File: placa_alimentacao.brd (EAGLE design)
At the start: 55.5 x 32.4 mm, 8 parts, among them IC1 7803TV

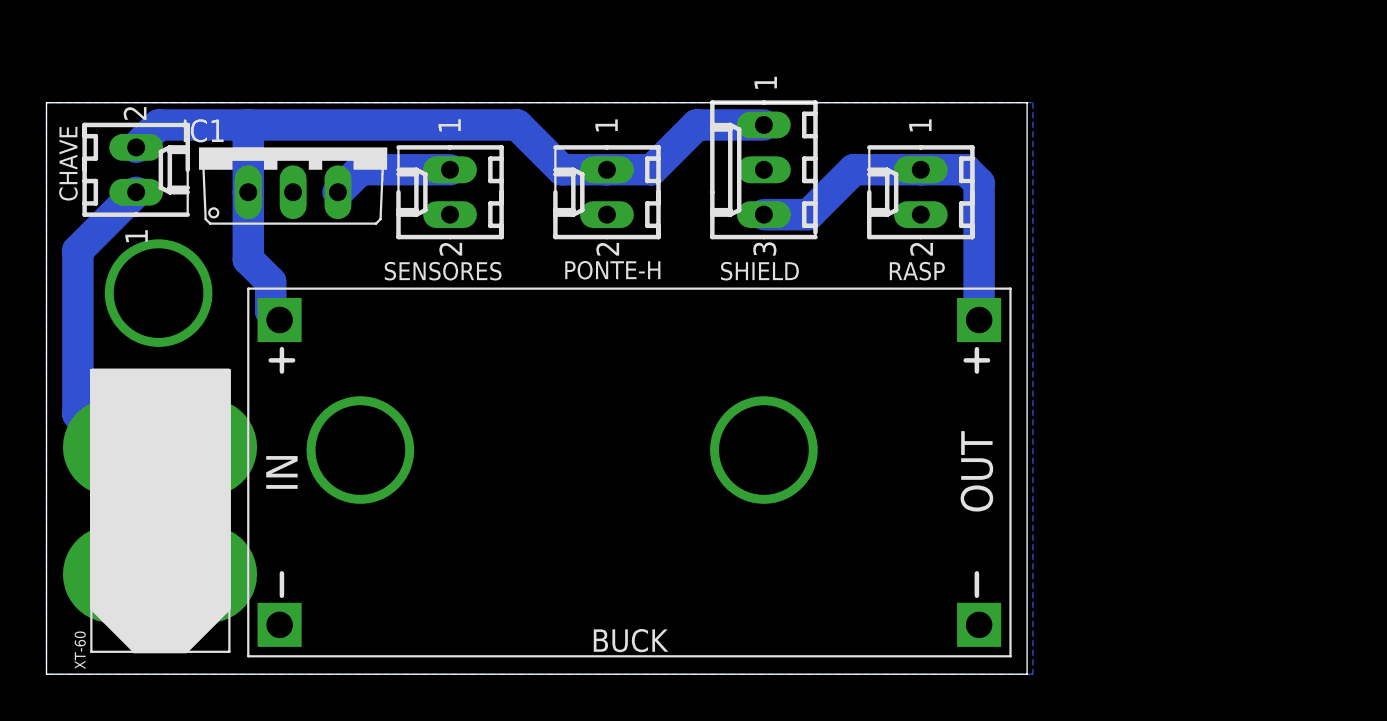
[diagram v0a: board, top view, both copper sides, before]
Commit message: Adicionado regulador de tensão
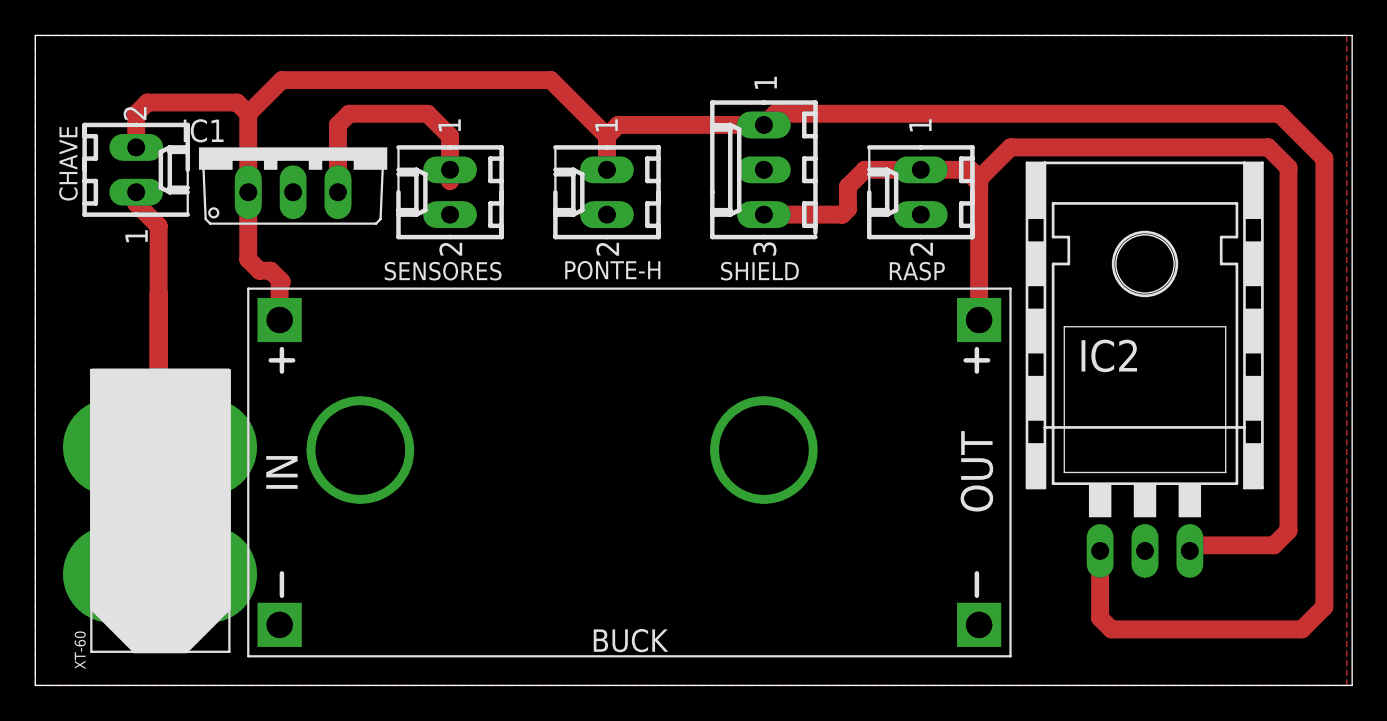
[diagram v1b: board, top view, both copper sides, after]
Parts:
- added IC2: (no value), 78xx_with_heatsink:78XXH
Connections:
- new net "": BUCK.IN+, CHAVE.2, IC1.1
- net +5V: now also IC2.OUT
- net +8V: now also IC2.IN; no longer BUCK.IN+, CHAVE.2, IC1.1, PONTE-H.1
- net GND: now also IC2.GND
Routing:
- net +5V: track 21.3 -> 74.8 mm
- net "": track 0.00 -> 44.6 mm
- net +8V: track 50.0 -> 86.8 mm
- net +5V/1: track 6.88 -> 14.1 mm
- net N$1: track 19.4 -> 25.3 mm
- added copper zone on layer 1, net S$1
- removed copper zone on layer 16, net GND
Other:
- board size 55.5 x 32.4 mm -> 74.6 x 36.8 mm

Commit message: Erro tirado
Schematic and board insconsistentes
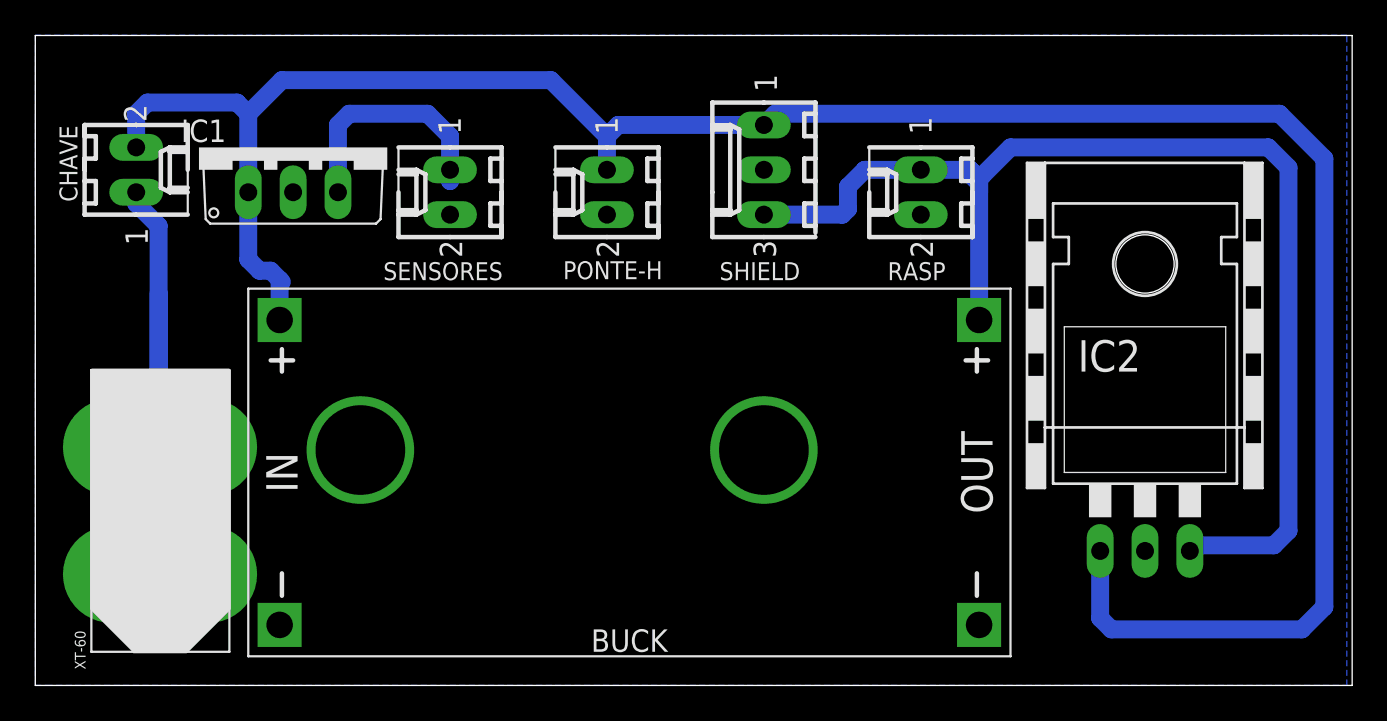
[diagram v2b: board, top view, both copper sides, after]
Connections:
- net +5V/1 renamed VCC
- removed net "": BUCK.IN+, CHAVE.2, IC1.1
- net +8V: now also BUCK.IN+, CHAVE.2, IC1.1, PONTE-H.1
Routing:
- net +8V: track 86.8 -> 131.4 mm
- net "": track 44.6 -> 0.00 mm
- net +5V: vias 0 -> 1
- added copper zone on layer 16, net GND
- removed copper zone on layer 1, net S$1
